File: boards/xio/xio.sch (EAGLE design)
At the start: 91 parts, among them U1 24 MHz Osc. (F535L-24), X1 PCI-E-164SOCKET, X2 PCI-E-164SOCKET, X3 PCI-E-164SOCKET, X4 PCI-E-164SOCKET, X5 PCI-E-164SOCKET, X6 PCI-E-164SOCKET, X7 PCI-E-164SOCKET

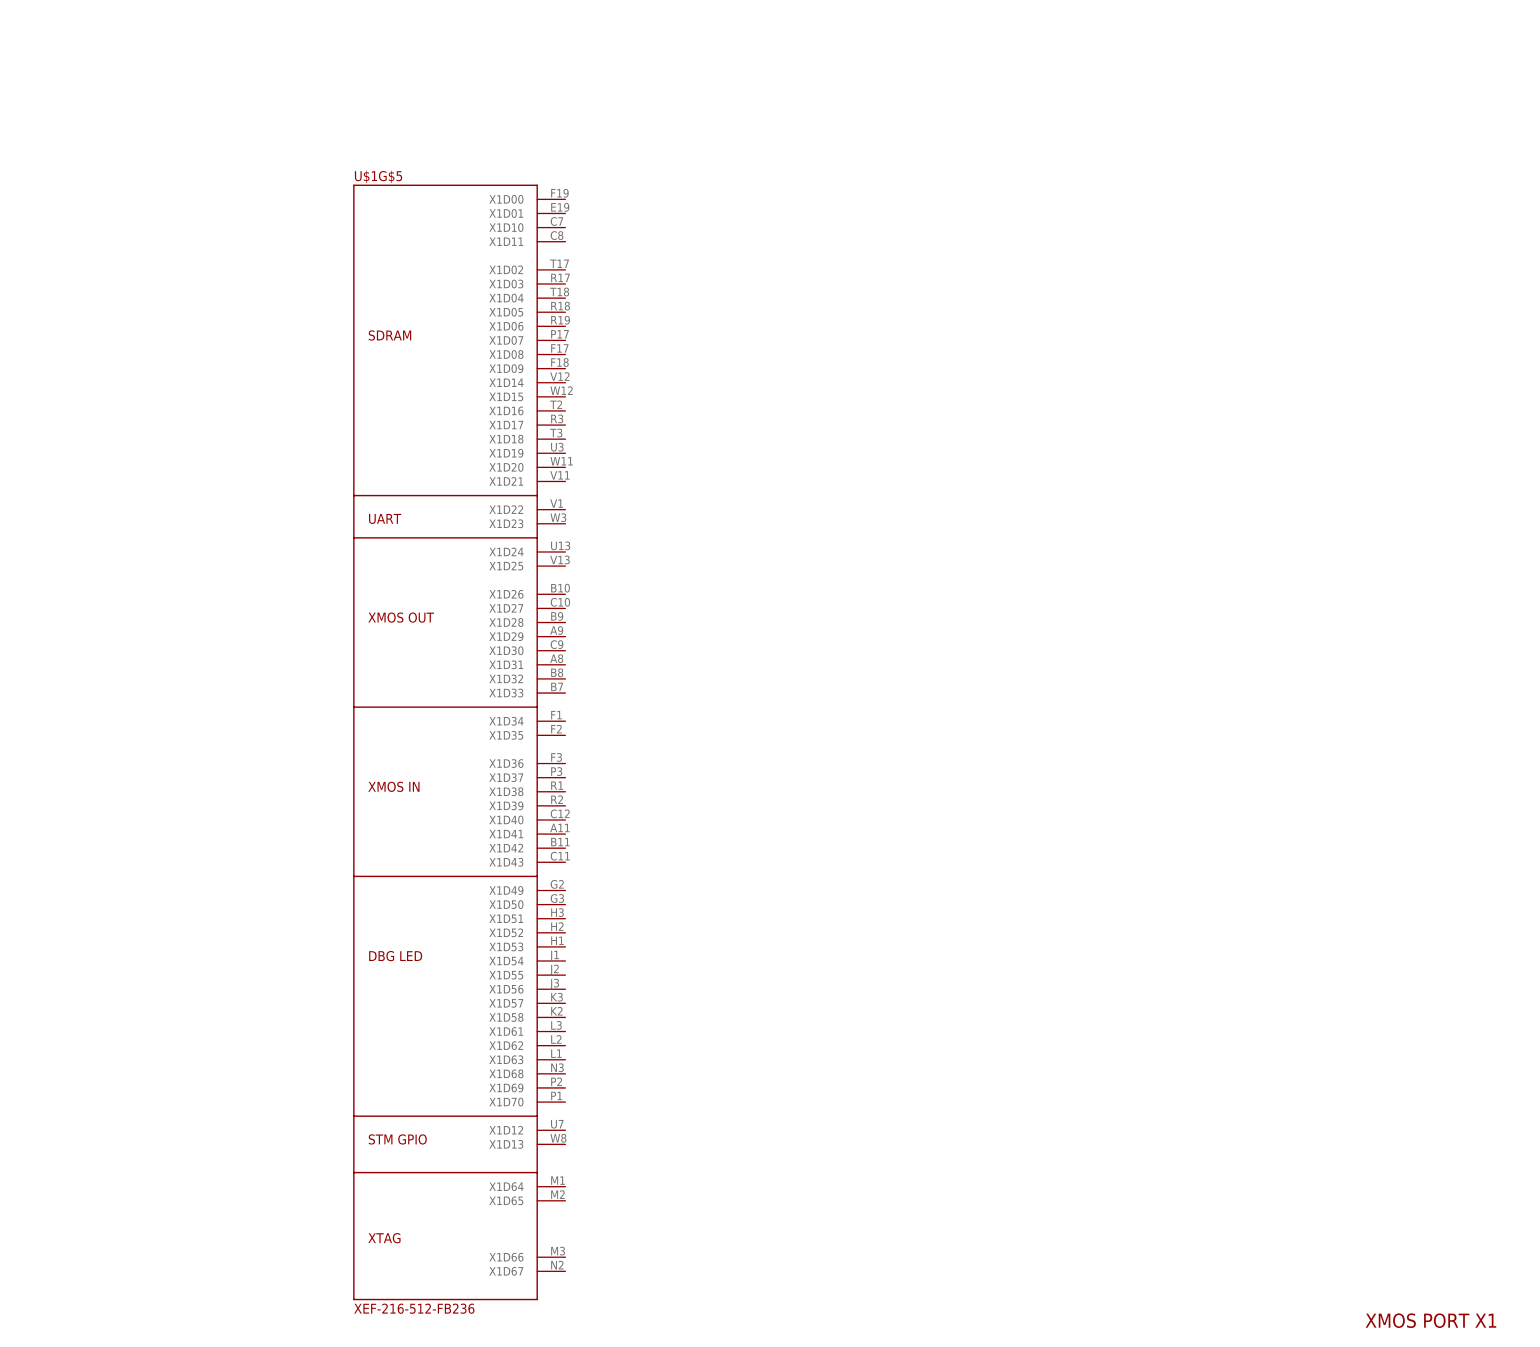
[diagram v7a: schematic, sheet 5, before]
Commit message: Start on the XMOS SDRAM
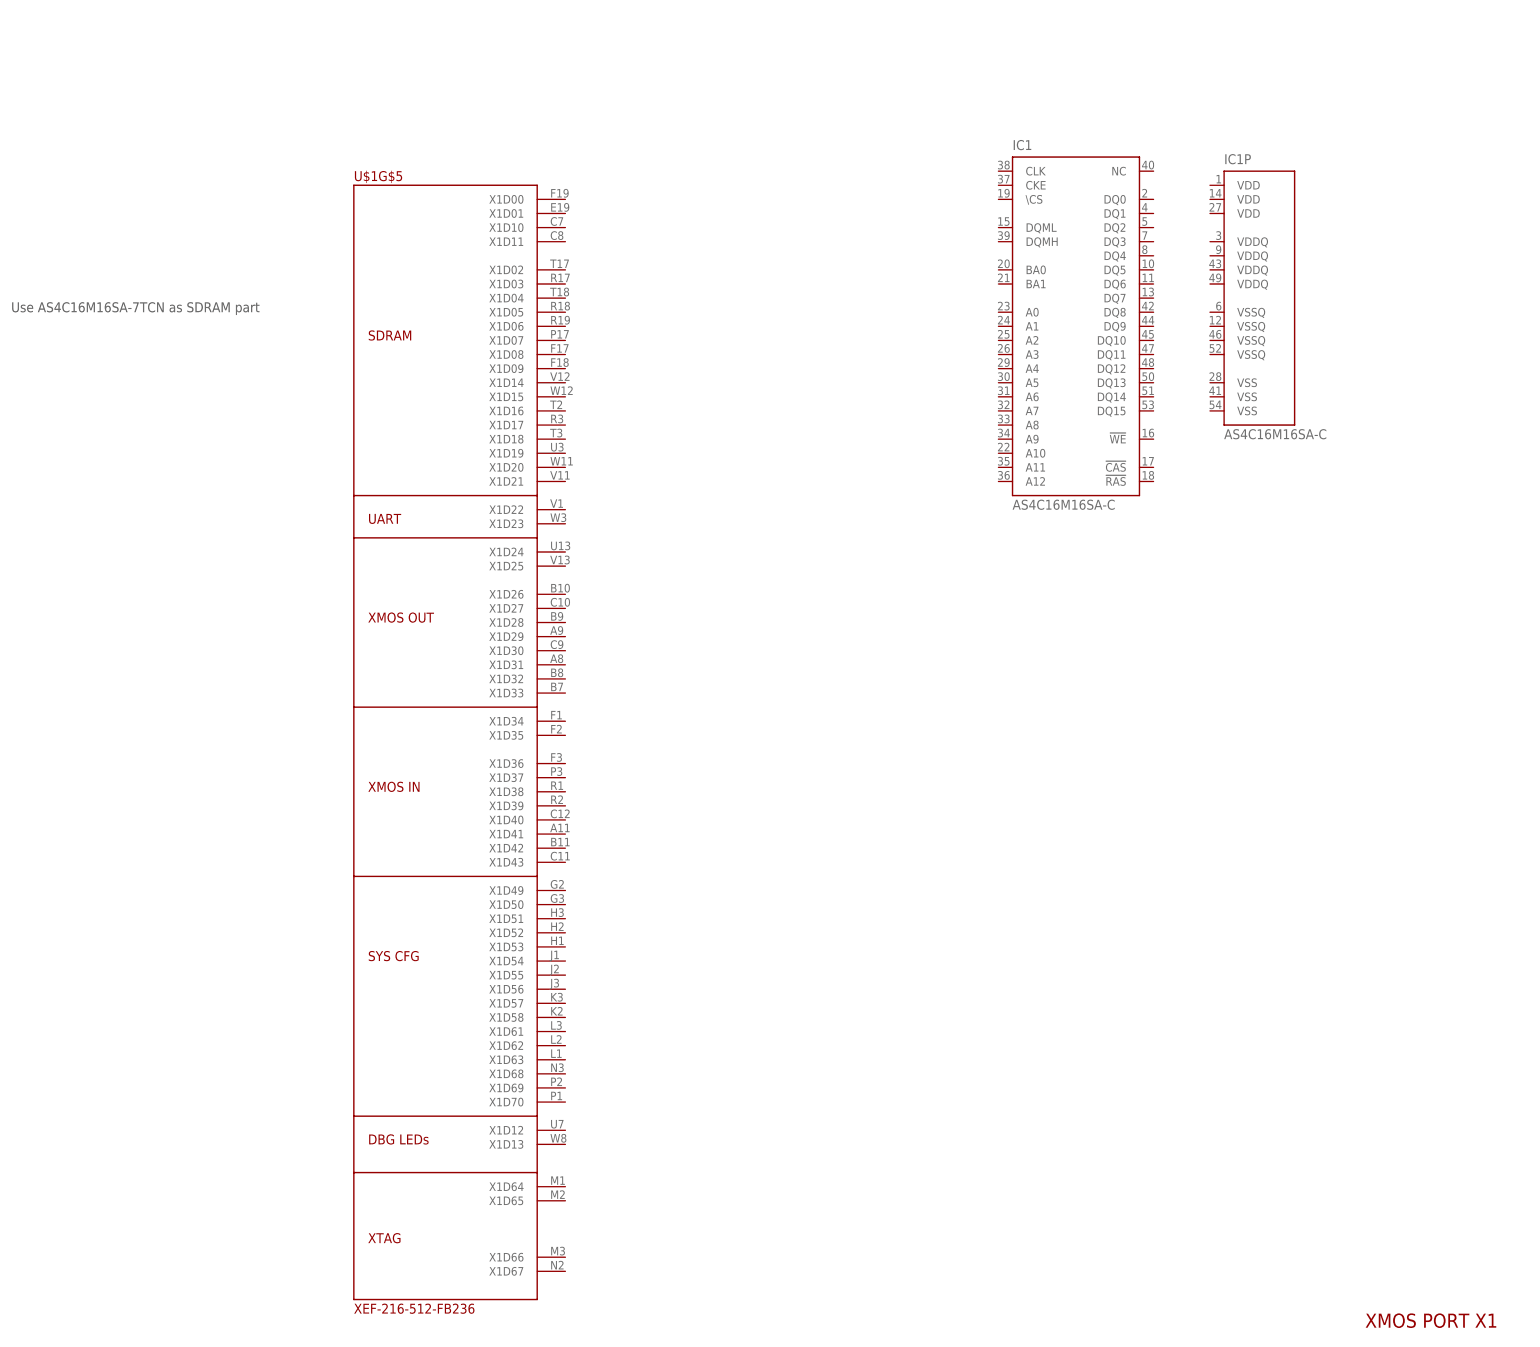
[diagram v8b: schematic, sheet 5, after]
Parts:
- added IC1: AS4C16M16SA-C, memory-micron:MT48LC16M16A2
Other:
- note added: "Use AS4C16M16SA-7TCN as SDRAM part"
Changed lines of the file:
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@@
 <setting verticaltext="up"/>
 </settings>
-<grid distance="0.1" unitdist="inch" unit="inch" style="lines" multiple="1" display="yes" altdistance="0.01" altunitdist="inch" altunit="inch"/>
+<grid distance="0.1" unitdist="inch" unit="inch" style="lines" multiple="1" display="no" altdistance="0.01" altunitdist="inch" altunit="inch"/>
 <layers>
 <layer number="1" name="Top" color="4" fill="1" visible="no" active="no"/>
@@
 <part name="R8" library="rcl" library_urn="urn:adsk.eagle:library:334" deviceset="R-EU_" device="R0402" package3d_urn="urn:adsk.eagle:package:23547/2" value="47k"/>
 <part name="R9" library="rcl" library_urn="urn:adsk.eagle:library:334" deviceset="R-EU_" device="R0402" package3d_urn="urn:adsk.eagle:package:23547/2" value="47k"/>
+<part name="IC1" library="memory-micron" library_urn="urn:adsk.eagle:library:274" deviceset="MT48LC16M16A2" device="" package3d_urn="urn:adsk.eagle:package:18739/1" value="AS4C16M16SA-C"/>
 </parts>
 <sheets>
@@
 <plain>
 <text x="165.1" y="-109.22" size="2.54" layer="94">XMOS PORT X1</text>
+<text x="-78.74" y="73.66" size="1.778" layer="97">Use AS4C16M16SA-7TCN as SDRAM part</text>
 </plain>
 <instances>
 <instance part="U$1" gate="G$5" x="0.762" y="0"/>
 <instance part="FRAME5" gate="G$1" x="-177.8" y="-129.54"/>
+<instance part="IC1" gate="G$1" x="111.76" y="73.66"/>
+<instance part="IC1" gate="P" x="144.78" y="76.2"/>
 </instances>
 <busses>
